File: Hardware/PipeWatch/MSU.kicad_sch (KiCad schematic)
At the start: 3 parts, among them U4 LIS3DHTR_C15134

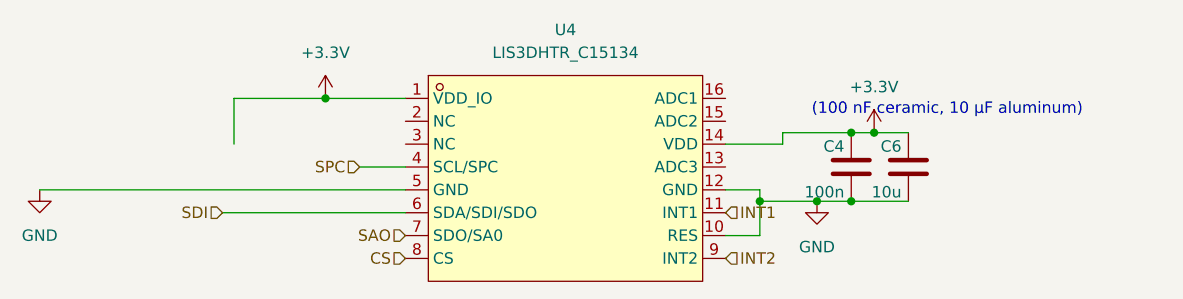
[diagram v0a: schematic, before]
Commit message: added Binky parts and a load of 3d references
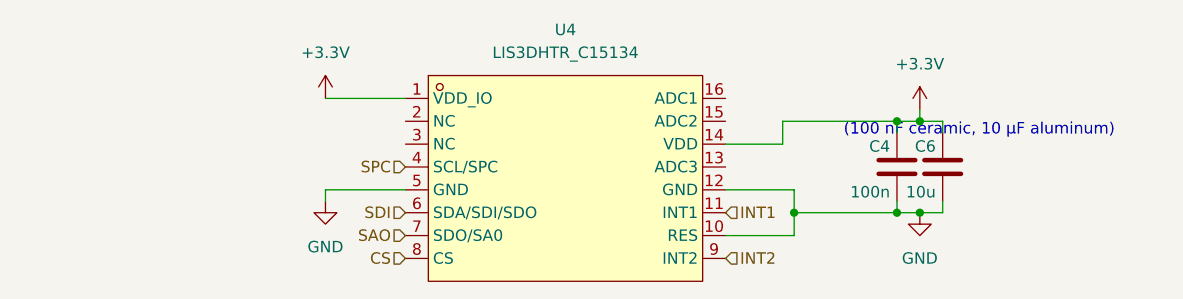
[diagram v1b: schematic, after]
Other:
- moved on the sheet: C4, C6

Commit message: some changes
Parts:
- C6: footprint Capacitor_SMD:C_0603_1608Metric -> Capacitor_SMD:CP_Elec_4x5.8
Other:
- note removed: "(100 nF ceramic, 10 μF aluminum)"
- moved on the sheet: C6
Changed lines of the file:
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@@
 	(generator_version "9.0")
 	(paper "A4")
-	(text "(100 nF ceramic, 10 μF aluminum)"
-		(exclude_from_sim no)
-		(at 184.404 93.726 0)
-		(effects
-			(font
-				(size 1.27 1.27)
-			)
-		)
-	)
 	(junction
 		(at 163.83 102.87)
@@
 	(wire
 		(pts
-			(xy 177.8 102.87) (xy 180.34 102.87)
+			(xy 177.8 102.87) (xy 181.61 102.87)
 		)
 		(stroke
@@
 	(wire
 		(pts
-			(xy 177.8 92.71) (xy 180.34 92.71)
+			(xy 177.8 92.71) (xy 181.61 92.71)
 		)
 		(stroke
@@
 	(wire
 		(pts
-			(xy 180.34 102.87) (xy 180.34 101.6)
+			(xy 181.61 102.87) (xy 181.61 101.6)
 		)
 		(stroke
@@
 	(wire
 		(pts
-			(xy 180.34 92.71) (xy 180.34 93.98)
+			(xy 181.61 92.71) (xy 181.61 93.98)
 		)
 		(stroke
@@
 	(symbol
 		(lib_id "Device:C")
-		(at 180.34 97.79 180)
+		(at 181.61 97.79 180)
 		(unit 1)
 		(exclude_from_sim no)
@@
 		(dnp no)
 		(property "Reference" "C6"
-			(at 179.578 95.504 0)
+			(at 180.848 95.504 0)
 			(effects
 				(font
@@
 		)
 		(property "Value" "10u"
-			(at 179.578 100.584 0)
+			(at 180.848 100.584 0)
 			(effects
 				(font
@@
 			)
 		)
-		(property "Footprint" "Capacitor_SMD:C_0603_1608Metric"
-			(at 179.3748 93.98 0)
+		(property "Footprint" "Capacitor_SMD:CP_Elec_4x5.8"
+			(at 180.6448 93.98 0)
 			(effects
 				(font
@@
 		)
 		(property "Datasheet" "~"
-			(at 180.34 97.79 0)
+			(at 181.61 97.79 0)
 			(effects
 				(font
@@
 		)
 		(property "Description" "Unpolarized capacitor"
-			(at 180.34 97.79 0)
-			(effects
-				(font
+			(at 181.61 97.79 0)
+			(effects
+				(font

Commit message: Changed the scematic page Labeling
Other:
- company: (none) -> Felix Pelster
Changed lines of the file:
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@@
 	(generator_version "9.0")
 	(paper "A4")
+	(title_block
+		(date "2025-09-24")
+		(company "Felix Pelster")
+	)
 	(junction
 		(at 163.83 102.87)
